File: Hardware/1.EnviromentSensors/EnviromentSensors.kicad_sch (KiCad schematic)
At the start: 14 parts, among them J2 Conn_01x05_Pin, U1 SHT4x, U2 BME680, U3 LPS22HB

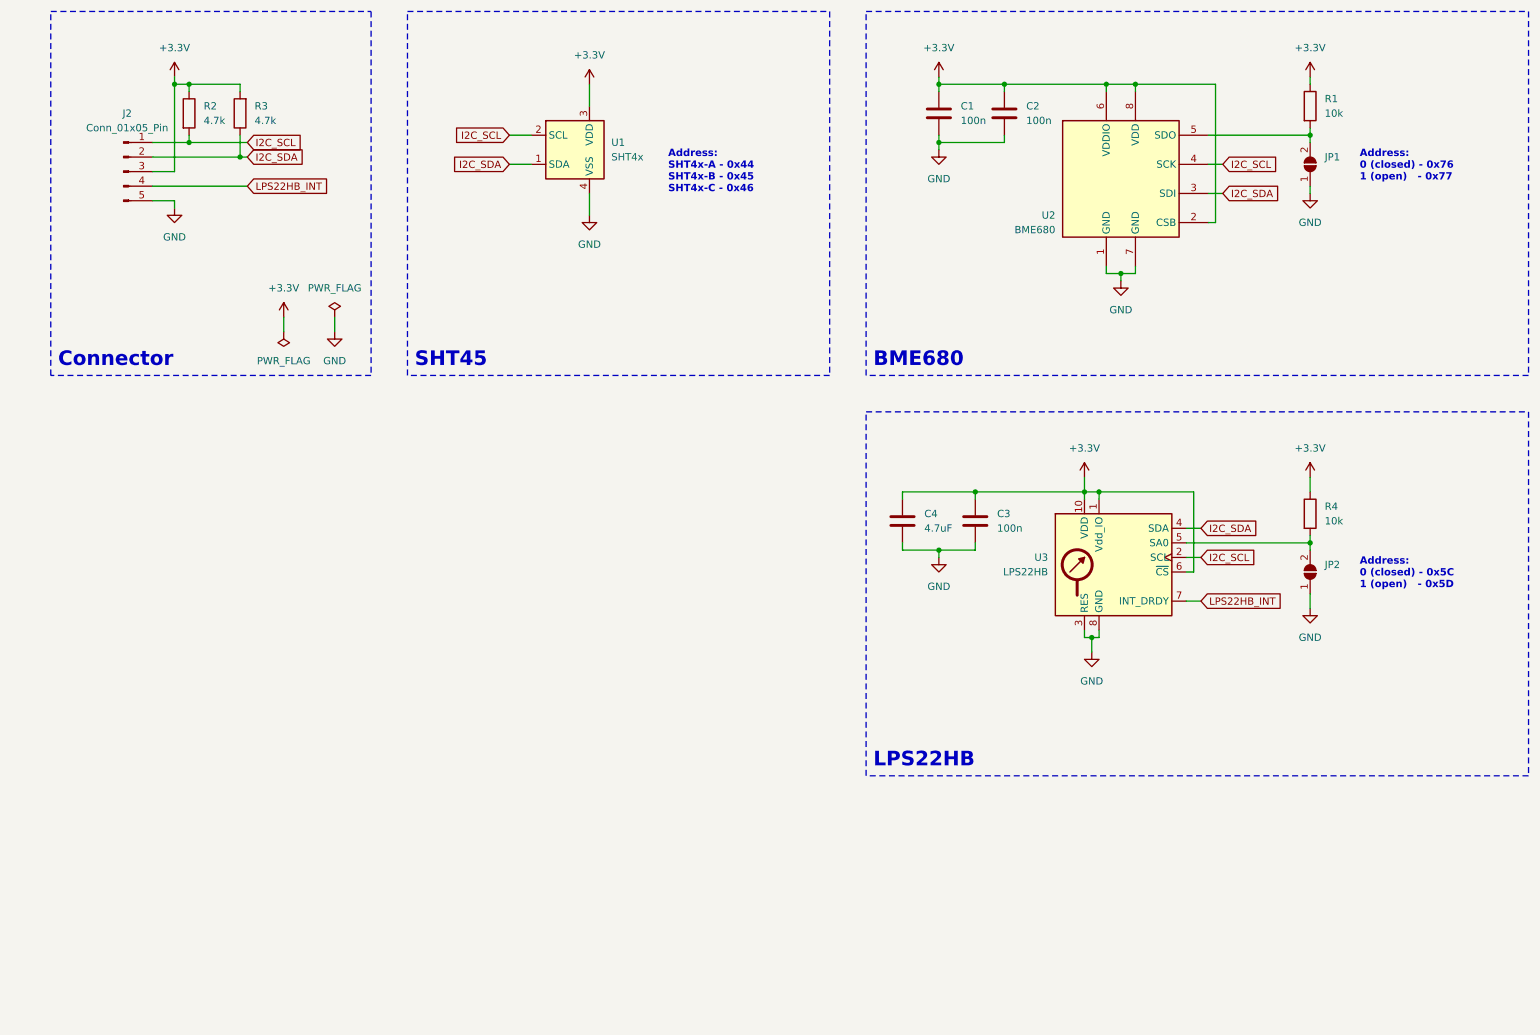
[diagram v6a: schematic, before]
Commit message: Add connector for LightSensors board
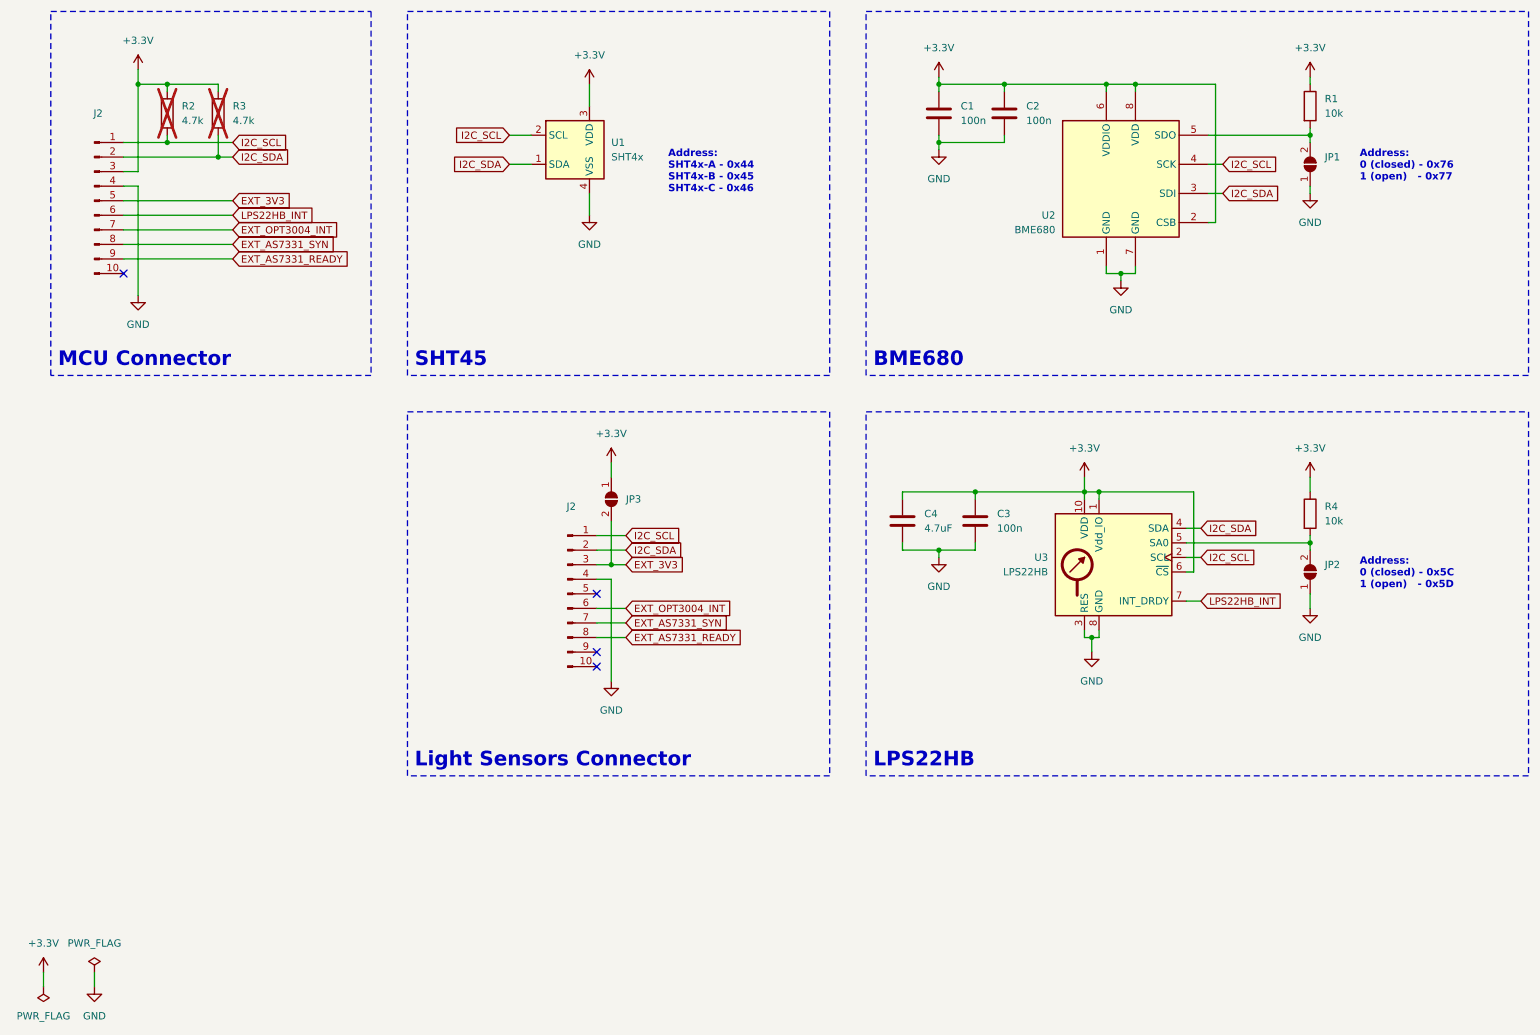
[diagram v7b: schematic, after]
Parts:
- removed J2: Conn_01x05_Pin, Connector_JST:JST_PH_S5B-PH-K_1x05_P2.00mm_Horizontal, symbol Connector:Conn_01x05_Pin
- added J2: Conn_01x10_Pin, Connector_JST:JST_PH_B10B-PH-K_1x10_P2.00mm_Vertical, symbol Connector:Conn_01x10_Pin
- added J2: Conn_01x10_Pin, Connector_JST:JST_PH_S10B-PH-K_1x10_P2.00mm_Horizontal, symbol Connector:Conn_01x10_Pin
- added JP3: SolderJumper_2_Open, Jumper:SolderJumper-2_P1.3mm_Open_TrianglePad1.0x1.5mm, symbol Jumper:SolderJumper_2_Open
- R2, R3: now not fitted
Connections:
- net +3.3V: now also J2.3 (Pin_3), JP3.1 (A)
- net GND: now also J2.4 (Pin_4), J2.4 (Pin_4)
- net I2C_SCL: now also J2.1 (Pin_1), J2.1 (Pin_1)
- net I2C_SDA: now also J2.2 (Pin_2), J2.2 (Pin_2)
- net LPS22HB_INT: now also J2.6 (Pin_6)
- new net EXT_3V3: J2.3 (Pin_3), J2.5 (Pin_5), JP3.2 (B)
- new net EXT_AS7331_READY: J2.8 (Pin_8), J2.9 (Pin_9)
- new net EXT_AS7331_SYN: J2.7 (Pin_7), J2.8 (Pin_8)
- new net EXT_OPT3004_INT: J2.6 (Pin_6), J2.7 (Pin_7)
- no-connect marks 0 -> 4
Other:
- note added: "Light Sensors Connector"
- note added: "MCU Connector"
- note removed: "Connector"
